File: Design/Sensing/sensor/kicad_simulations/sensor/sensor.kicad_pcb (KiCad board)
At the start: 2 copper layers, 61.2 x 37.5 mm, 38 parts, among them J1 Conn_01x02_Pin, J10 Conn_01x02_Pin, J11 Conn_01x02_Pin, J12 Conn_01x02_Pin, J13 Conn_01x02_Pin, J14 Conn_01x01_Pin, J15 Conn_01x01_Pin, J16 Conn_01x02_Pin, J17 Conn_01x02_Pin, J2 Conn_01x02_Pin, J3 Conn_02x14_Counter_Clockwise, J5 L_S_B, J6 Conn_01x01_Pin, J7 Conn_01x02_Pin, J8 Conn_01x02_Pin, J9 Conn_01x02_Pin, Q1 MMBT5551L, Q2 MMBT5551L, Q3 MMBT5551L, U1 LM324, U2 TSSP58038, U3 TSSP58038, U4 TSSP58038

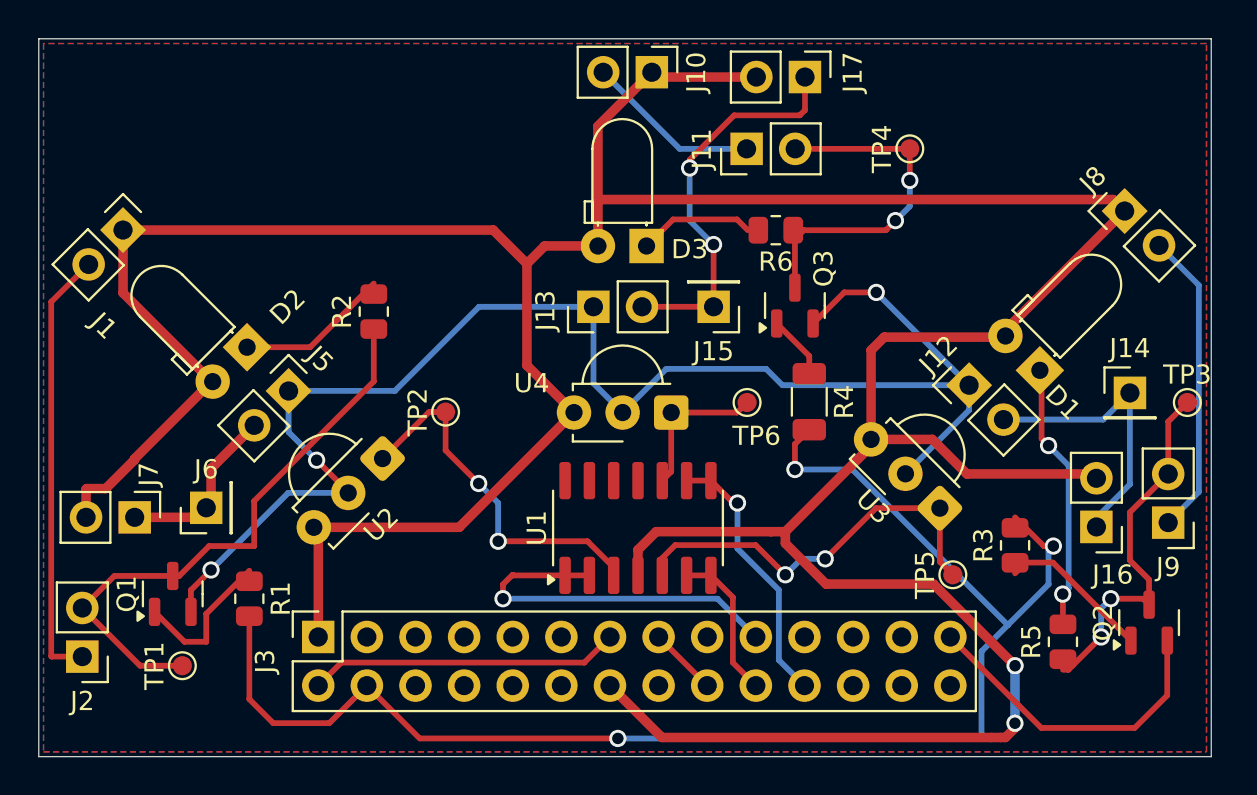
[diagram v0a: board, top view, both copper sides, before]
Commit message: ensured that net names in the connectors matches the label in th project
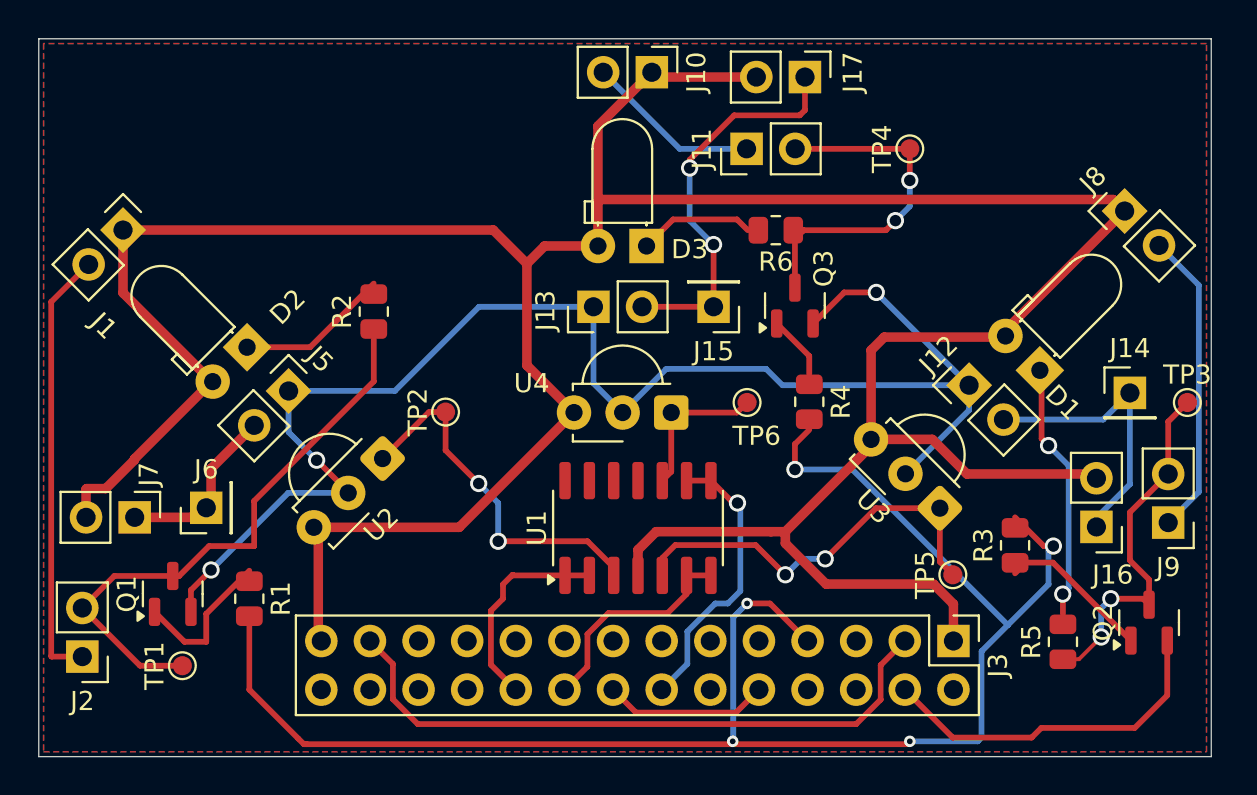
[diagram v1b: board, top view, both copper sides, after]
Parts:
- J3: value Conn_02x14_Counter_Clockwise -> Conn_02x14_Odd_Even; footprint Connector_PinSocket_2.54mm:PinSocket_2x14_P2.54mm_Vertical -> Connector_PinHeader_2.54mm:PinHeader_2x14_P2.54mm_Vertical
- R4: footprint Resistor_SMD:R_1206_3216Metric -> Resistor_SMD:R_0805_2012Metric
- moved J3 33.2 mm to (156.8, 106.5), turned to -90 degrees
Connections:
- J3 pad 10: /PE9 -> GND
- J3 pad 11: /PE8 -> /PE13
- J3 pad 12: /RESV1 -> /PA5
- J3 pad 13: /BATT -> /PE12
- J3 pad 14: /3V3 -> /PA6
- J3 pad 15: GND -> /PE11
- J3 pad 16: /AB0 -> GND
- J3 pad 17: /PC5 -> /PA10
- J3 pad 18: GND -> /PA7
- J3 pad 19: /PC4 -> /PE9
- J3 pad 2: /BATT -> /RESV3
- J3 pad 20: /PA7 -> /PC4
- J3 pad 21: GND -> /PE8
- J3 pad 22: /PA6 -> GND
- J3 pad 23: /PA5 -> /RESV1
- J3 pad 24: GND -> /PC5
- J3 pad 25: /PA4 -> /BATT
- J3 pad 26: /PA3 -> /AB0
- J3 pad 27: GND -> /3V3
- J3 pad 28: /RESV3 -> GND
- J3 pad 3: /RESV2 -> /BATT
- J3 pad 4: /PE15 -> GND
- J3 pad 5: /PE14 -> /RESV2
- J3 pad 6: /PA13 -> /PA3
- J3 pad 7: /PE12 -> /PE15
- J3 pad 8: /PE11 -> /PA4
- J3 pad 9: /PA10 -> /PE14
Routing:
- net /3V3: track 211.0 -> 182.6 mm, vias 2 -> 0
- net /BATT: track 16.3 -> 33.7 mm
- net /PE15: track 75.6 -> 85.9 mm, vias 3 -> 5
- net /PC4: track 19.5 -> 11.0 mm, vias 1 -> 0
- net GND: track 98.7 -> 105.3 mm
- net /PA7: track 8.00 -> 11.7 mm
- net /PA6: track 14.1 -> 15.0 mm

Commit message: ensured that net names in the connectors matches the label in th project
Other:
- board text added: "Zwivhuya Ndou NDXZWI002 EEE3088F SENSOR BOARD"
